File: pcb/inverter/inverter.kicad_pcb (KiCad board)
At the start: 4 copper layers, 100 x 61.5 mm, 44 parts, among them J1 Conn_01x01_Female, J2 Conn_01x01_Female, J3 Conn_01x01_Female, J4 Conn_01x01_Female, J5 Conn_01x02_Male, J6 Conn_01x02_Male, J7 Conn_01x02_Male, J8 Conn_01x02_Male, Q1 IRG4PF50W, Q2 IRG4PF50W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

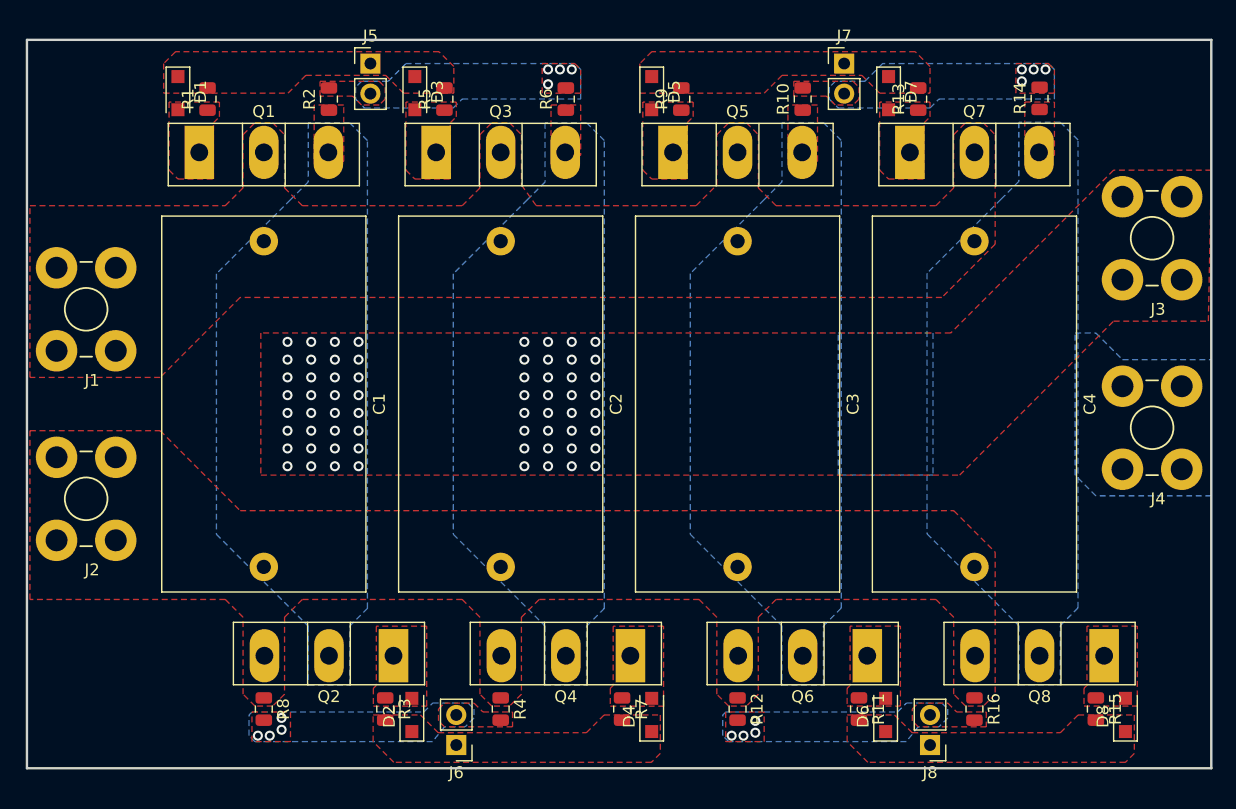
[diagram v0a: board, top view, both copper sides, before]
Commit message: inverter PCB layout finished
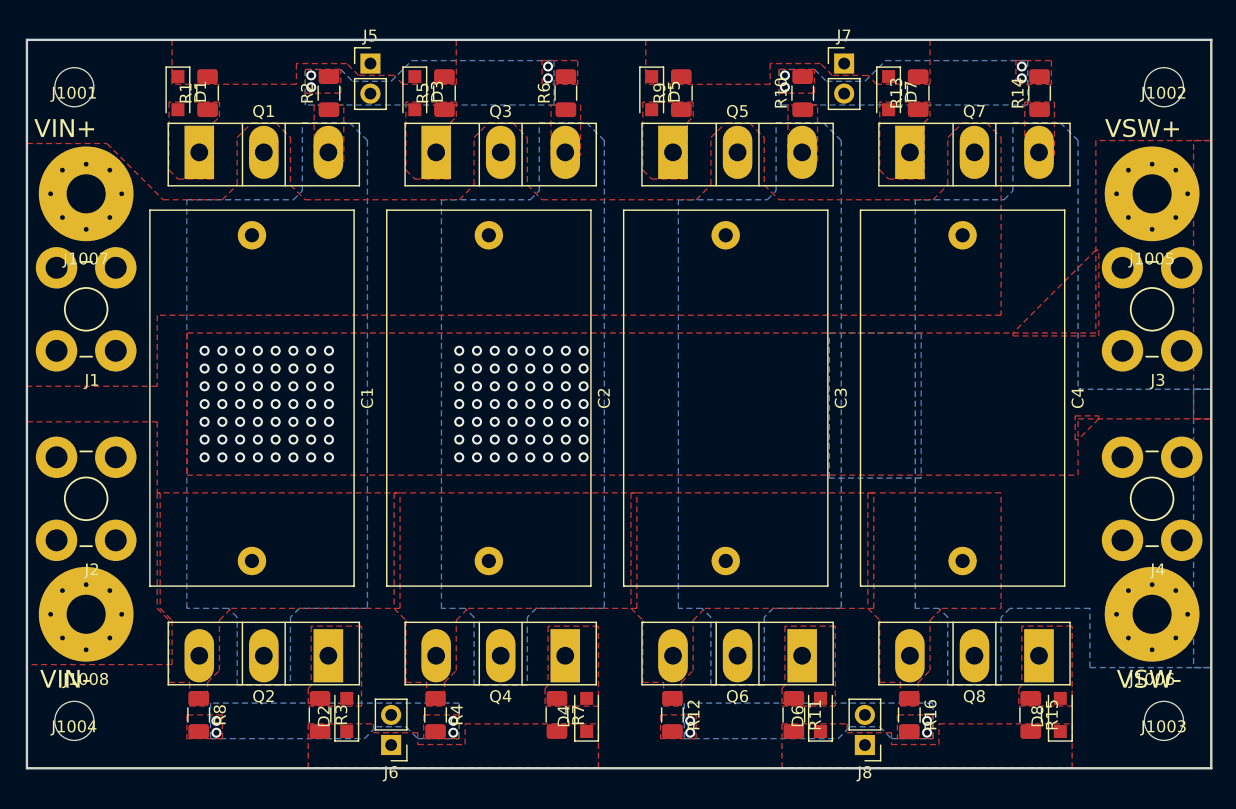
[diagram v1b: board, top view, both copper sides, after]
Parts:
- added J1001: mounting-hole-nc, wbraun_smd:M3-through-hole, F.Cu at (104.5, 49.5)
- added J1002: mounting-hole-nc, wbraun_smd:M3-through-hole, F.Cu at (196.5, 49.5)
- added J1003: mounting-hole-nc, wbraun_smd:M3-through-hole, F.Cu at (196.5, 103.0)
- added J1004: mounting-hole-nc, wbraun_smd:M3-through-hole, F.Cu at (104.5, 103.0)
- added J1005: mounting-hole-grounded, wbraun_smd:M3-tight-fit-pan-head, F.Cu at (195.5, 58.5)
- added J1006: mounting-hole-grounded, wbraun_smd:M3-tight-fit-pan-head, F.Cu at (195.5, 94.0)
- added J1007: mounting-hole-grounded, wbraun_smd:M3-tight-fit-pan-head, F.Cu at (105.5, 58.5)
- added J1008: mounting-hole-grounded, wbraun_smd:M3-tight-fit-pan-head, F.Cu at (105.5, 94.0)
- R1, R10, R11, R12, R13, R14, R15, R16, R2, R3, R4, R5, R6, R7, R8, R9: footprint Resistor_SMD:R_0805_2012Metric -> Resistor_SMD:R_1206_3216Metric
- moved J3 6.00 mm to (195.5, 68.2)
- moved J4 6.00 mm to (195.5, 84.2)
- moved R11 5.52 mm to (165.2, 102.5)
- moved R12 5.52 mm to (155.0, 102.5)
- moved R15 5.52 mm to (185.2, 102.5)
- moved R16 5.52 mm to (175.0, 102.5)
- moved R3 5.52 mm to (125.2, 102.5)
- moved R4 5.52 mm to (135.0, 102.5)
- moved R7 5.52 mm to (145.2, 102.5)
- moved R8 5.52 mm to (115.0, 102.5)
- moved D2 5.50 mm to (127.5, 102.5)
- moved D4 5.50 mm to (147.8, 102.5)
- moved D6 5.50 mm to (167.5, 102.5)
- moved D8 5.50 mm to (187.8, 102.5)
- moved J6 5.50 mm to (131.2, 105.0)
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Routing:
- net /VSW+: vias 64 -> 112
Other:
- rule pad_to_mask_clearance: 0.2 -> 0.075
- board text added: "Cute QCW Inverter Board wdb@stanford.edu"
- board text added: "VIN+"
- board text added: "VIN-"
- board text added: "VSW+"
- board text added: "VSW-"

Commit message: created inverter gerbers
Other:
- copper layers 4 -> 2
- board text added: "Git Commit Hash: e5b1fa94865fde49c8e613bb4f34355756f7bcc4 https://github.com/westonb/cute-qcw"
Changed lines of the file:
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@@
   (general
     (thickness 1.6)
-    (drawings 10)
+    (drawings 11)
     (tracks 128)
     (zones 0)
@@
   (layers
     (0 F.Cu signal)
-    (1 In1.Cu signal hide)
-    (2 In2.Cu signal hide)
     (31 B.Cu signal)
     (32 B.Adhes user)
@@
     (visible_elements FFF9FF7F)
     (pcbplotparams
-      (layerselection 0x010fc_ffffffff)
+      (layerselection 0x010f0_ffffffff)
       (usegerberextensions false)
       (usegerberattributes false)
@@
       (psnegative false)
       (psa4output false)
-      (plotreference true)
-      (plotvalue true)
+      (plotreference false)
+      (plotvalue false)
       (plotinvisibletext false)
       (padsonsilk false)
@@
       (outputformat 1)
       (mirror false)
-      (drillshape 1)
+      (drillshape 0)
       (scaleselection 1)
-      (outputdirectory ""))
+      (outputdirectory "../../gerbers/inverter/"))
   )
   (net 0 "")
@@
     )
   )
+  (gr_text "Git Commit Hash:\ne5b1fa94865fde49c8e613bb4f34355756f7bcc4\nhttps://github.com/westonb/cute-qcw" (at 170.25 82) (layer B.SilkS)
+    (effects (font (size 0.8 0.8) (thickness 0.15)) (justify mirror))
+  )
   (gr_text "Cute QCW Inverter Board\nwdb@stanford.edu" (at 171.5 76.25) (layer B.SilkS)

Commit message: regenerated all gerbers and ordered controller and inverter pcbs
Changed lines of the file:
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@@
-(kicad_pcb (version 20171130) (host pcbnew "(5.0.1-3-g963ef8bb5)")
+(kicad_pcb (version 20171130) (host pcbnew 5.0.2-bee76a0~70~ubuntu18.04.1)
   (general
     (thickness 1.6)
@@
   )
   (zone (net 6) (net_name /VSW+) (layer F.Cu) (hatch edge 0.508)
-    (connect_pads yes (clearance 1))
-    (min_thickness 0.254)
-    (fill yes (arc_segments 16) (thermal_gap 0.508) (thermal_bridge_width 0.508))
-    (polygon
-      (pts
-        (xy 191 63.25) (xy 190.75 63.25) (xy 183.75 70.25) (xy 183.75 70.5) (xy 191 70.5)
-      )
-    )
-  )
-  (zone (net 6) (net_name /VSW+) (layer F.Cu) (hatch edge 0.508)
     (connect_pads yes (clearance 0.25))
     (min_thickness 0.2)
@@
       )
     )
+  )
+  (zone (net 0) (net_name "") (layer B.Cu) (hatch edge 0.508)
+    (connect_pads (clearance 0.49))
+    (min_thickness 0.254)
+    (keepout (tracks allowed) (vias allowed) (copperpour not_allowed))
+    (fill (arc_segments 16) (thermal_gap 0.508) (thermal_bridge_width 0.508))
+    (polygon
+      (pts
+        (xy 190.25 93.5) (xy 190.25 89.5) (xy 189.25 89.5) (xy 189.25 93.5)
+      )
+    )
+  )
+  (zone (net 6) (net_name /VSW+) (layer F.Cu) (hatch edge 0.508)
+    (connect_pads yes (clearance 0.49))
+    (min_thickness 0.254)
+    (fill yes (arc_segments 16) (thermal_gap 0.508) (thermal_bridge_width 0.508))
+    (polygon
+      (pts
+        (xy 184.25 68.75) (xy 184.25 59) (xy 191 59) (xy 191 70.5) (xy 184.25 70.5)
+      )
+    )
